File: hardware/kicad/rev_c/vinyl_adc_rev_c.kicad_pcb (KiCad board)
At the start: 4 copper layers, 170 x 120 mm, 119 parts, among them J1 CLK SEL, J2 RASPBERRY PI 4, J20 LINE IN L, J60 LINE IN R, U1 74HC244, U2 LM358, U20 TL072, U21 LM311, U22 TL072, U23 74HC74, U24 74HC04, U3 74HCT132, U4 74HC4040, U6 74HC157, U60 TL072, U61 LM311, U62 TL072, U63 74HC74, U64 74HC04, U8 74HC4049, U9 74HCU04, Y1 6.144MHz

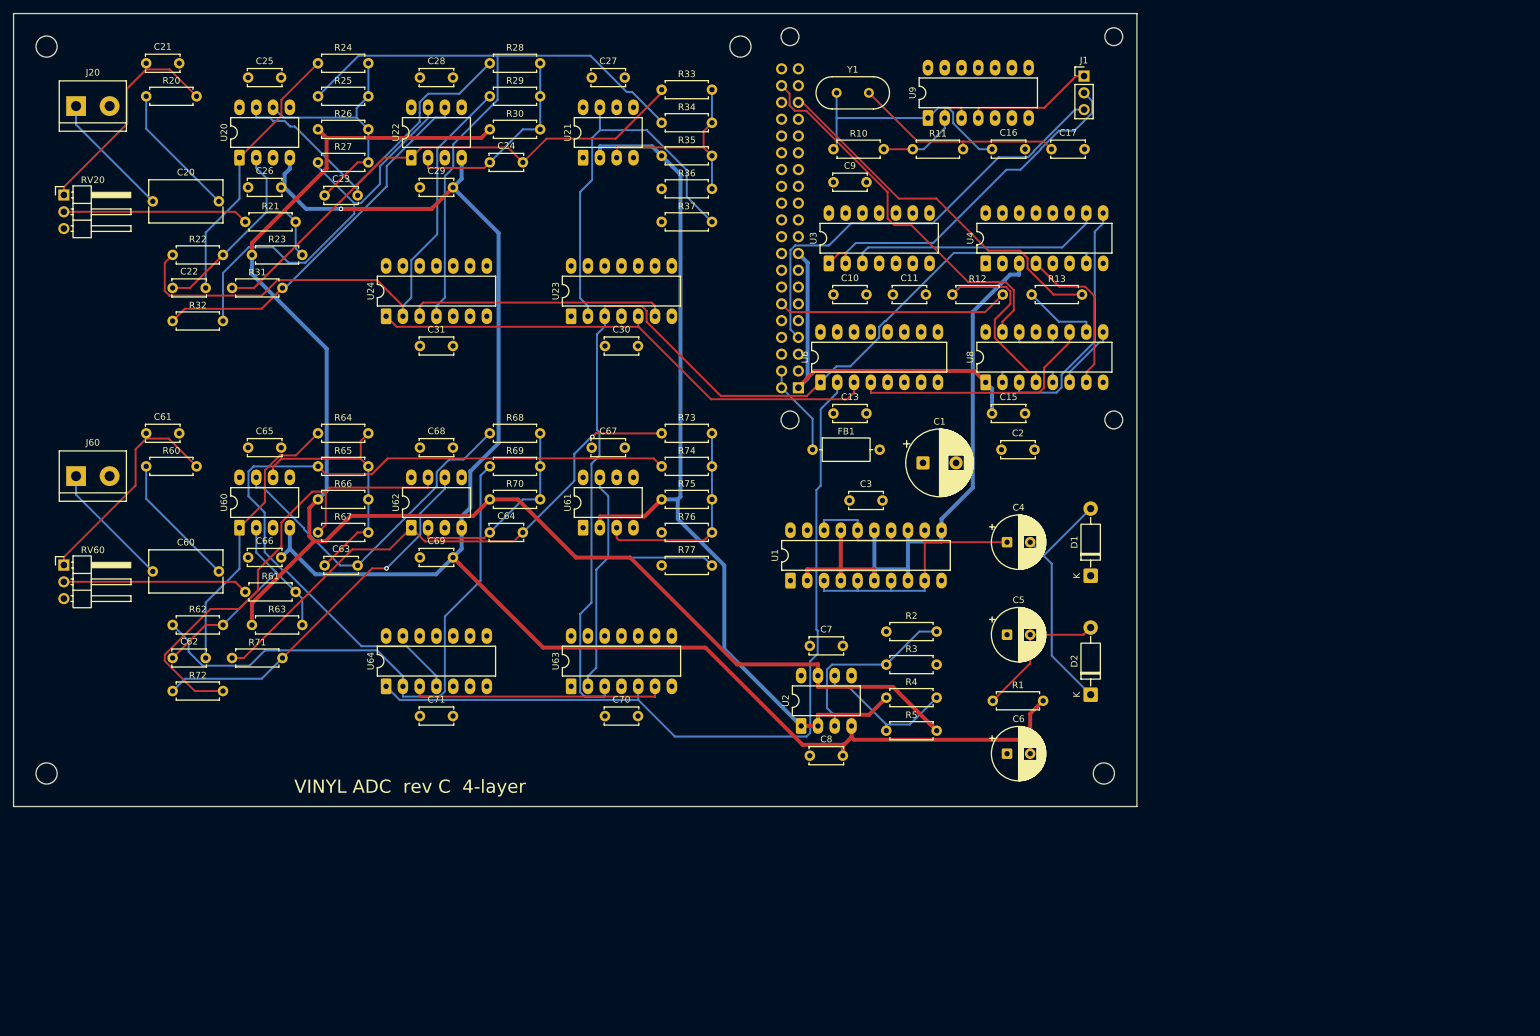
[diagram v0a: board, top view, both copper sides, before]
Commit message: Rev D enclosure, short v2 and channel L Gerbers
Rev D enclosure: CAD scripts, spec, print files (STL/3MF/STEP/DXF) and the
SolidCraft assembly with renders. Short v2: the Remotion project, voice/sfx
scripts and PCB layer art (renders, audio and footage stay local). Channel L
production Gerbers, bring-up log update and KiCad project tweaks.
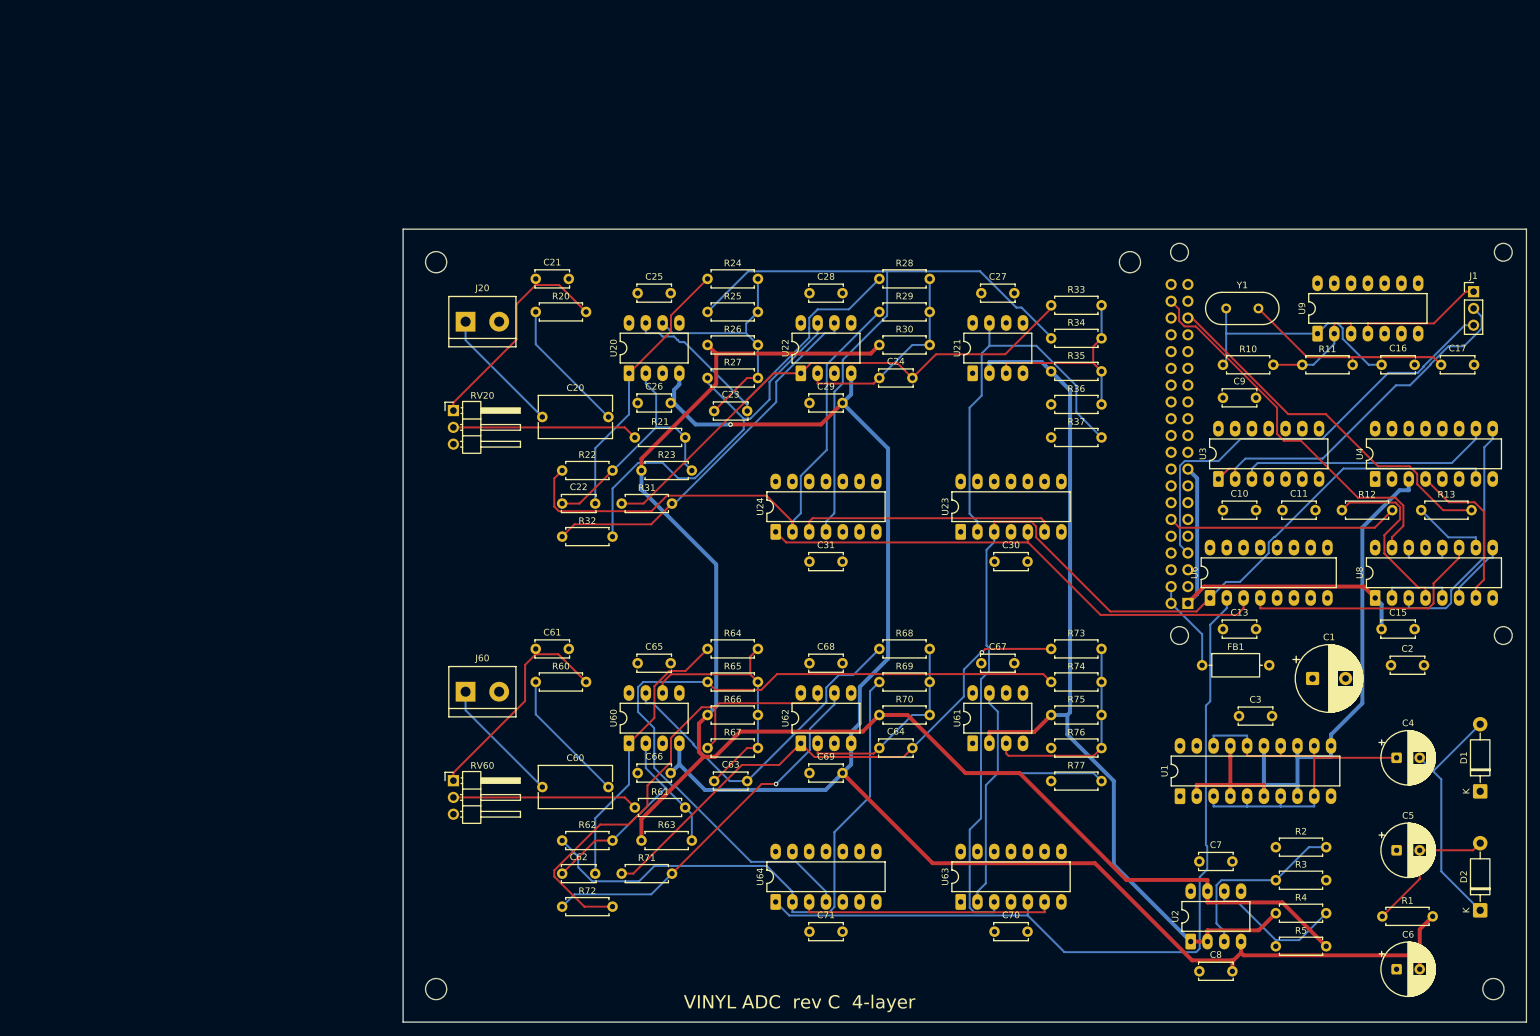
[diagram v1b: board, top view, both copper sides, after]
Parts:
- moved C11 67.4 mm to (192.0, 75.2)
- moved C15 67.4 mm to (207.0, 93.2)
- moved C16 67.4 mm to (207.0, 53.2)
- moved C17 67.4 mm to (216.0, 53.2)
- moved C21 67.4 mm to (79.0, 40.2)
- moved C22 67.4 mm to (83.0, 74.2)
- moved C23 67.4 mm to (106.0, 60.2)
- moved C25 67.4 mm to (94.4, 42.3)
- moved C27 67.4 mm to (146.4, 42.3)
- moved C28 67.4 mm to (120.4, 42.3)
- moved C6 67.4 mm to (209.3, 144.6)
- moved C61 67.4 mm to (79.0, 96.2)
- moved C7 67.4 mm to (179.4, 128.3)
- moved C70 67.4 mm to (148.4, 138.9)
- moved C71 67.4 mm to (120.4, 138.9)
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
